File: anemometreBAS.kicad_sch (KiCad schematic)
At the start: 12 parts, among them J1 Conn_01x03_Male, J2 Conn_01x02_Male, J3 Conn_01x02_Male, J4 Conn_01x02_Male, J5 Conn_01x02_Male, U1 TP4056

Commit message: fix error
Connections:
- net 3V3: now also R1.1
- net at J1.1 (Pin_1): now also R1.2, XA1.A1; no longer R1.1
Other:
- moved on the sheet: R1
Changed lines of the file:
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@@
 (kicad_sch (version 20211123) (generator eeschema)
   (paper "A4")
+  (junction (at 100.33 86.36) (diameter 0) (color 0 0 0 0)
+  )
   (junction (at 34.29 76.2) (diameter 0) (color 0 0 0 0)
   )
@@
   (junction (at 199.39 55.88) (diameter 0) (color 0 0 0 0)
   )
+  (wire (pts (xy 90.17 86.36) (xy 92.71 86.36))
+    (stroke (width 0) (type default) (color 0 0 0 0))
+  )
+  (wire (pts (xy 199.39 55.88) (xy 208.28 55.88))
+    (stroke (width 0) (type default) (color 0 0 0 0))
+  )
+  (wire (pts (xy 76.2 113.03) (xy 83.82 113.03))
+    (stroke (width 0) (type default) (color 0 0 0 0))
+  )
+  (wire (pts (xy 34.29 60.96) (xy 34.29 66.04))
+    (stroke (width 0) (type default) (color 0 0 0 0))
+  )
+  (wire (pts (xy 205.74 58.42) (xy 208.28 58.42))
+    (stroke (width 0) (type default) (color 0 0 0 0))
+  )
+  (wire (pts (xy 34.29 76.2) (xy 38.1 76.2))
+    (stroke (width 0) (type default) (color 0 0 0 0))
+  )
+  (wire (pts (xy 118.11 109.22) (xy 123.19 109.22))
+    (stroke (width 0) (type default) (color 0 0 0 0))
+  )
+  (wire (pts (xy 34.29 86.36) (xy 34.29 91.44))
+    (stroke (width 0) (type default) (color 0 0 0 0))
+  )
+  (wire (pts (xy 101.6 104.14) (xy 123.19 104.14))
+    (stroke (width 0) (type default) (color 0 0 0 0))
+  )
+  (wire (pts (xy 76.2 115.57) (xy 83.82 115.57))
+    (stroke (width 0) (type default) (color 0 0 0 0))
+  )
+  (wire (pts (xy 120.65 78.74) (xy 123.19 78.74))
+    (stroke (width 0) (type default) (color 0 0 0 0))
+  )
+  (wire (pts (xy 80.01 125.73) (xy 83.82 125.73))
+    (stroke (width 0) (type default) (color 0 0 0 0))
+  )
+  (wire (pts (xy 97.79 64.77) (xy 97.79 67.31))
+    (stroke (width 0) (type default) (color 0 0 0 0))
+  )
+  (wire (pts (xy 120.65 73.66) (xy 123.19 73.66))
+    (stroke (width 0) (type default) (color 0 0 0 0))
+  )
+  (wire (pts (xy 189.23 55.88) (xy 199.39 55.88))
+    (stroke (width 0) (type default) (color 0 0 0 0))
+  )
+  (wire (pts (xy 60.96 40.64) (xy 60.96 44.45))
+    (stroke (width 0) (type default) (color 0 0 0 0))
+  )
+  (wire (pts (xy 199.39 40.64) (xy 199.39 48.26))
+    (stroke (width 0) (type default) (color 0 0 0 0))
+  )
+  (wire (pts (xy 72.39 128.27) (xy 83.82 128.27))
+    (stroke (width 0) (type default) (color 0 0 0 0))
+  )
+  (wire (pts (xy 109.22 106.68) (xy 123.19 106.68))
+    (stroke (width 0) (type default) (color 0 0 0 0))
+  )
+  (wire (pts (xy 85.09 40.64) (xy 85.09 38.1))
+    (stroke (width 0) (type default) (color 0 0 0 0))
+  )
+  (wire (pts (xy 95.25 64.77) (xy 95.25 72.39))
+    (stroke (width 0) (type default) (color 0 0 0 0))
+  )
+  (wire (pts (xy 60.96 120.65) (xy 83.82 120.65))
+    (stroke (width 0) (type default) (color 0 0 0 0))
+  )
+  (wire (pts (xy 118.11 101.6) (xy 123.19 101.6))
+    (stroke (width 0) (type default) (color 0 0 0 0))
+  )
+  (wire (pts (xy 85.09 40.64) (xy 85.09 44.45))
+    (stroke (width 0) (type default) (color 0 0 0 0))
+  )
+  (wire (pts (xy 60.96 118.11) (xy 83.82 118.11))
+    (stroke (width 0) (type default) (color 0 0 0 0))
+  )
+  (wire (pts (xy 34.29 73.66) (xy 34.29 76.2))
+    (stroke (width 0) (type default) (color 0 0 0 0))
+  )
+  (wire (pts (xy 34.29 76.2) (xy 34.29 78.74))
+    (stroke (width 0) (type default) (color 0 0 0 0))
+  )
+  (wire (pts (xy 63.5 40.64) (xy 85.09 40.64))
+    (stroke (width 0) (type default) (color 0 0 0 0))
+  )
+  (wire (pts (xy 85.09 25.4) (xy 85.09 30.48))
+    (stroke (width 0) (type default) (color 0 0 0 0))
+  )
+  (wire (pts (xy 100.33 64.77) (xy 100.33 86.36))
+    (stroke (width 0) (type default) (color 0 0 0 0))
+  )
   (wire (pts (xy 100.33 86.36) (xy 123.19 86.36))
-    (stroke (width 0) (type default) (color 0 0 0 0))
-  )
-  (wire (pts (xy 199.39 55.88) (xy 208.28 55.88))
-    (stroke (width 0) (type default) (color 0 0 0 0))
-  )
-  (wire (pts (xy 76.2 113.03) (xy 83.82 113.03))
-    (stroke (width 0) (type default) (color 0 0 0 0))
-  )
-  (wire (pts (xy 34.29 60.96) (xy 34.29 66.04))
-    (stroke (width 0) (type default) (color 0 0 0 0))
-  )
-  (wire (pts (xy 205.74 58.42) (xy 208.28 58.42))
-    (stroke (width 0) (type default) (color 0 0 0 0))
-  )
-  (wire (pts (xy 34.29 76.2) (xy 38.1 76.2))
-    (stroke (width 0) (type default) (color 0 0 0 0))
-  )
-  (wire (pts (xy 118.11 109.22) (xy 123.19 109.22))
-    (stroke (width 0) (type default) (color 0 0 0 0))
-  )
-  (wire (pts (xy 34.29 86.36) (xy 34.29 91.44))
-    (stroke (width 0) (type default) (color 0 0 0 0))
-  )
-  (wire (pts (xy 101.6 104.14) (xy 123.19 104.14))
-    (stroke (width 0) (type default) (color 0 0 0 0))
-  )
-  (wire (pts (xy 76.2 115.57) (xy 83.82 115.57))
-    (stroke (width 0) (type default) (color 0 0 0 0))
-  )
-  (wire (pts (xy 120.65 78.74) (xy 123.19 78.74))
-    (stroke (width 0) (type default) (color 0 0 0 0))
-  )
-  (wire (pts (xy 80.01 125.73) (xy 83.82 125.73))
-    (stroke (width 0) (type default) (color 0 0 0 0))
-  )
-  (wire (pts (xy 97.79 64.77) (xy 97.79 68.58))
-    (stroke (width 0) (type default) (color 0 0 0 0))
-  )
-  (wire (pts (xy 120.65 73.66) (xy 123.19 73.66))
-    (stroke (width 0) (type default) (color 0 0 0 0))
-  )
-  (wire (pts (xy 189.23 55.88) (xy 199.39 55.88))
-    (stroke (width 0) (type default) (color 0 0 0 0))
-  )
-  (wire (pts (xy 60.96 40.64) (xy 60.96 44.45))
-    (stroke (width 0) (type default) (color 0 0 0 0))
-  )
-  (wire (pts (xy 199.39 40.64) (xy 199.39 48.26))
-    (stroke (width 0) (type default) (color 0 0 0 0))
-  )
-  (wire (pts (xy 72.39 128.27) (xy 83.82 128.27))
-    (stroke (width 0) (type default) (color 0 0 0 0))
-  )
-  (wire (pts (xy 109.22 106.68) (xy 123.19 106.68))
-    (stroke (width 0) (type default) (color 0 0 0 0))
-  )
-  (wire (pts (xy 85.09 40.64) (xy 85.09 38.1))
-    (stroke (width 0) (type default) (color 0 0 0 0))
-  )
-  (wire (pts (xy 95.25 64.77) (xy 95.25 73.66))
-    (stroke (width 0) (type default) (color 0 0 0 0))
-  )
-  (wire (pts (xy 60.96 120.65) (xy 83.82 120.65))
-    (stroke (width 0) (type default) (color 0 0 0 0))
-  )
-  (wire (pts (xy 118.11 101.6) (xy 123.19 101.6))
-    (stroke (width 0) (type default) (color 0 0 0 0))
-  )
-  (wire (pts (xy 85.09 40.64) (xy 85.09 44.45))
-    (stroke (width 0) (type default) (color 0 0 0 0))
-  )
-  (wire (pts (xy 60.96 118.11) (xy 83.82 118.11))
-    (stroke (width 0) (type default) (color 0 0 0 0))
-  )
-  (wire (pts (xy 34.29 73.66) (xy 34.29 76.2))
-    (stroke (width 0) (type default) (color 0 0 0 0))
-  )
-  (wire (pts (xy 34.29 76.2) (xy 34.29 78.74))
-    (stroke (width 0) (type default) (color 0 0 0 0))
-  )
-  (wire (pts (xy 100.33 64.77) (xy 100.33 78.74))
-    (stroke (width 0) (type default) (color 0 0 0 0))
-  )
-  (wire (pts (xy 63.5 40.64) (xy 85.09 40.64))
-    (stroke (width 0) (type default) (color 0 0 0 0))
-  )
-  (wire (pts (xy 85.09 25.4) (xy 85.09 30.48))
     (stroke (width 0) (type default) (color 0 0 0 0))
   )
@@
     )
   )
+  (global_label "3V3" (shape input) (at 90.17 86.36 180) (fields_autoplaced)
+    (effects (font (size 1.27 1.27)) (justify right))
+    (property "Intersheet References" "${INTERSHEET_REFS}" (id 0) (at 84.2493 86.4394 0)
+      (effects (font (size 1.27 1.27)) (justify left) hide)
+    )
+  )
   (global_label "VIN" (shape input) (at 80.01 125.73 180) (fields_autoplaced)
     (effects (font (size 1.27 1.27)) (justify right))
@@
     )
   )
-  (global_label "5V" (shape input) (at 97.79 68.58 270) (fields_autoplaced)
-    (effects (font (size 1.27 1.27)) (justify right))
-    (property "Intersheet References" "${INTERSHEET_REFS}" (id 0) (at 97.8694 73.2912 90)
+  (global_label "5V" (shape input) (at 97.79 67.31 270) (fields_autoplaced)
+    (effects (font (size 1.27 1.27)) (justify right))
+    (property "Intersheet References" "${INTERSHEET_REFS}" (id 0) (at 97.8694 72.0212 90)
       (effects (font (size 1.27 1.27)) (justify left) hide)
     )
@@
     )
   )
-  (global_label "GND" (shape input) (at 95.25 73.66 270) (fields_autoplaced)
-    (effects (font (size 1.27 1.27)) (justify right))
-    (property "Intersheet References" "${INTERSHEET_REFS}" (id 0) (at 95.3294 79.9436 90)
+  (global_label "GND" (shape input) (at 95.25 72.39 270) (fields_autoplaced)
+    (effects (font (size 1.27 1.27)) (justify right))
+    (property "Intersheet References" "${INTERSHEET_REFS}" (id 0) (at 95.3294 78.6736 90)
       (effects (font (size 1.27 1.27)) (justify left) hide)
     )
@@
     (pin "2")
   )
-  (symbol (lib_id "Device:R") (at 100.33 82.55 0) (unit 1)
-    (in_bom yes) (on_board yes) (fields_autoplaced)
-    (property "Reference" "R1" (id 0) (at 102.87 81.2799 0)
-      (effects (font (size 1.27 1.27)) (justify left))
-    )
-    (property "Value" "4.7K" (id 1) (at 102.87 83.8199 0)
-      (effects (font (size 1.27 1.27)) (justify left))
-    )
-    (property "Footprint" "" (id 2) (at 98.552 82.55 90)
-      (effects (font (size 1.27 1.27)) hide)
-    )
-    (property "Datasheet" "~" (id 3) (at 100.33 82.55 0)
-      (effects (font (size 1.27 1.27)) hide)
-    )
+  (symbol (lib_id "Device:R") (at 96.52 86.36 90) (unit 1)
+    (in_bom yes) (on_board yes) (fields_autoplaced)
+    (property "Reference" "R1" (id 0) (at 96.52 80.01 90))
+    (property "Value" "4.7K" (id 1) (at 96.52 82.55 90))
+    (property "Footprint" "" (id 2) (at 96.52 88.138 90)
+      (effects (font (size 1.27 1.27)) hide)
+    )
+    (property "Datasheet" "~" (id 3) (at 96.52 86.36 0)
+      (effects (font (size 1.27 1.27)) hide)
+    )

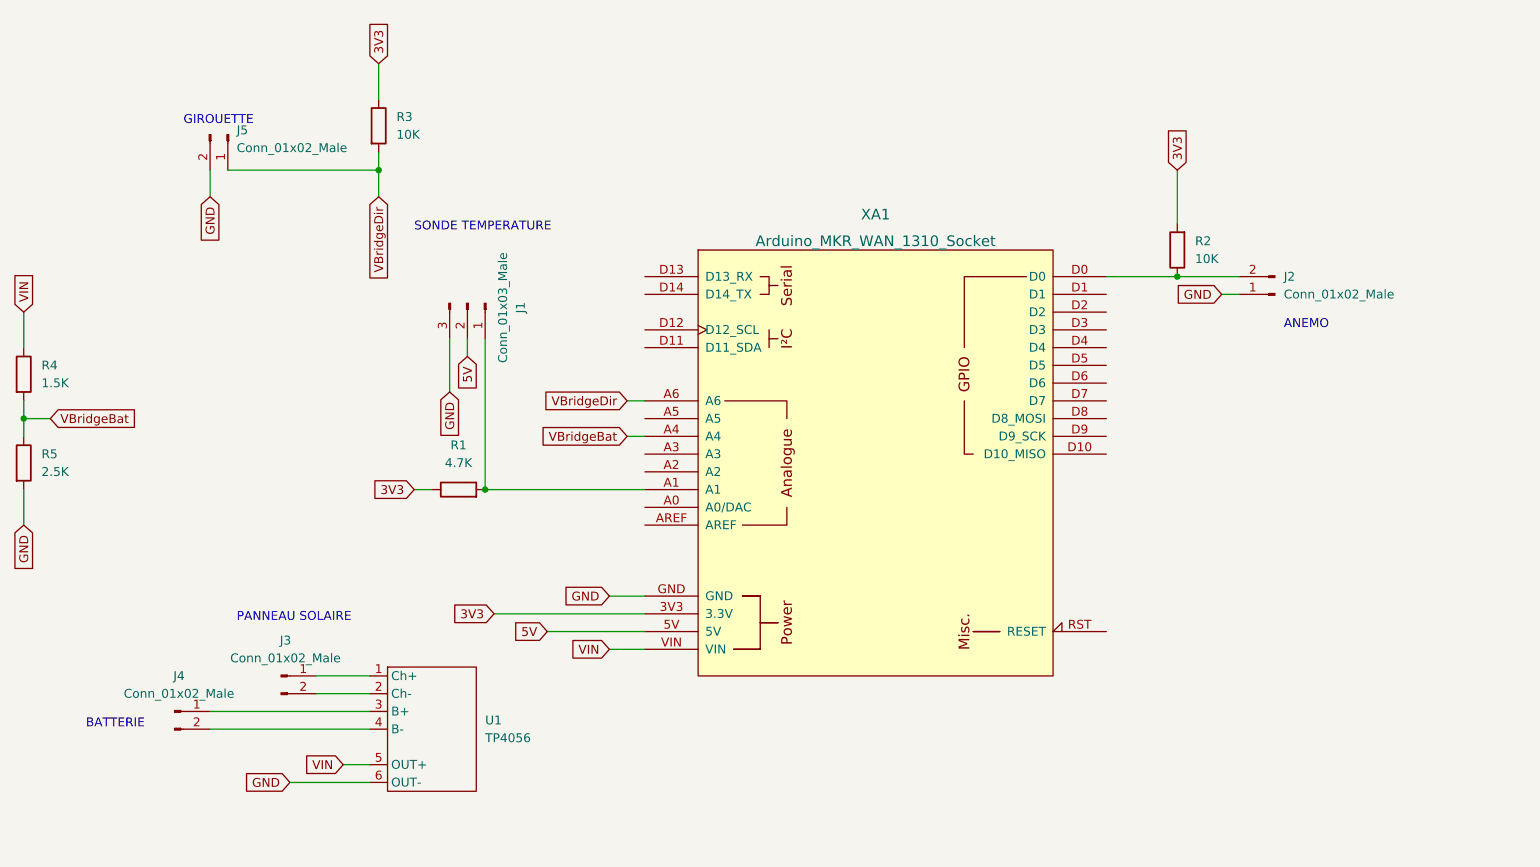
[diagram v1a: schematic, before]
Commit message: Pcb traversant (#1)
* first pcb version with schematic footprint update

* schematic
	GND at the same pin for each connector
	add M3 hole*3 connected to GND
PCB
	first routing

* Adding 3D model

* route temp sensor data
change +5V net location
change hole location
drc ok only one error with hole under mkr processing board

* pcb without smd resistor
first routing version

* change layer of solar panel and battery mngt card
unshow $Reference and value

* Adding pins socket connectors for MKR1310

* adding optionnal CEM schottky diode
MKR 3D model update

* update 3D models with MKR pin shocket

---------

Co-authored-by: sdaviet <sylvain.daviet@gmail.com>
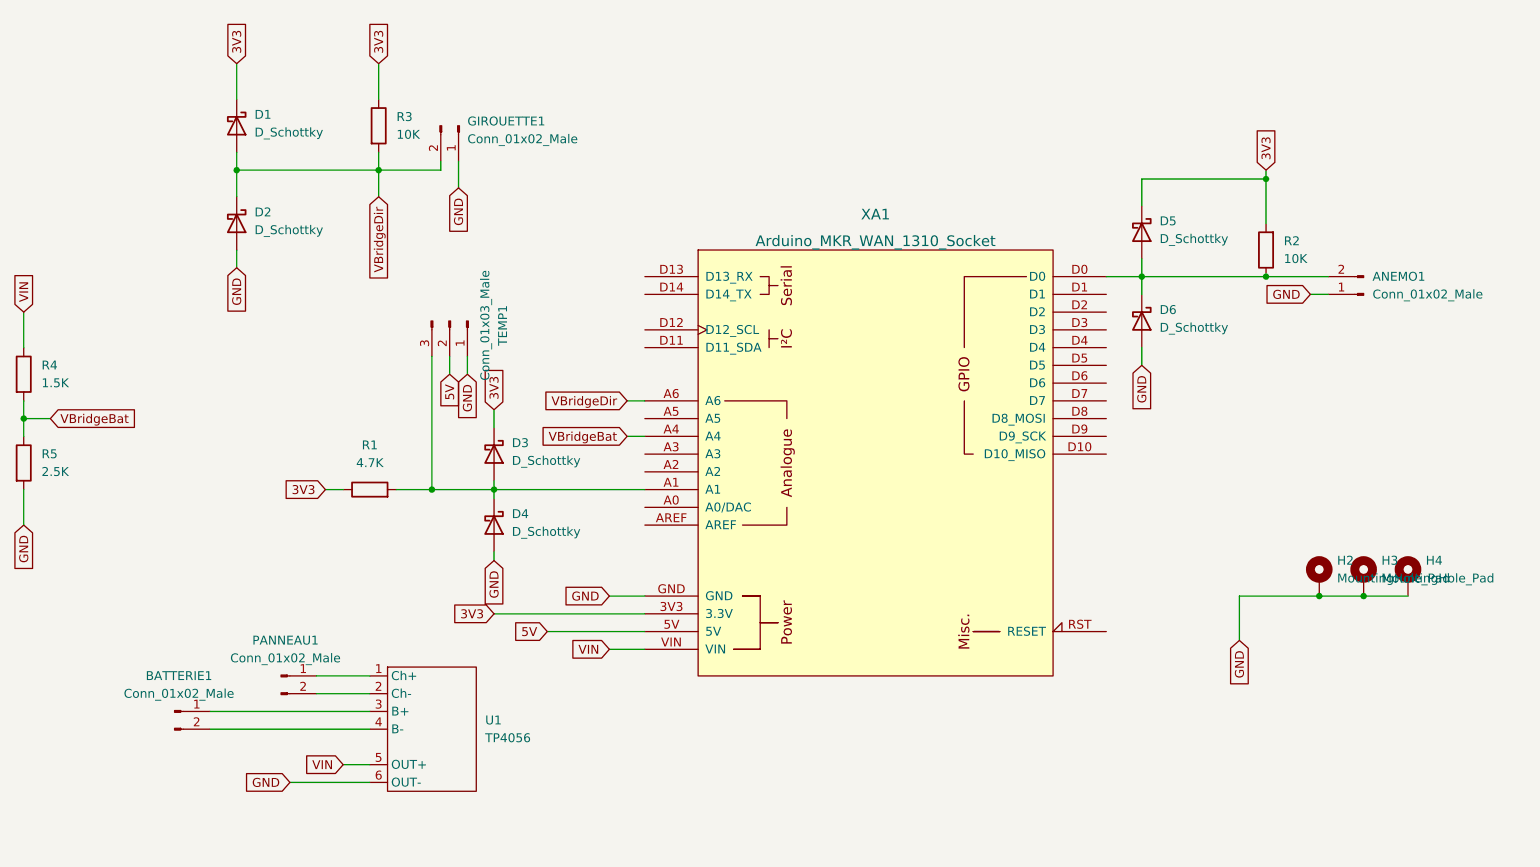
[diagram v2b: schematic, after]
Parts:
- added D1, D2, D3, D4, D5, D6: D_Schottky, Diode_THT:D_DO-35_SOD27_P7.62mm_Horizontal, symbol Device:D_Schottky
- added H2, H3, H4: MountingHole_Pad, MountingHole:MountingHole_3.2mm_M3_Pad_TopBottom, symbol Mechanical:MountingHole_Pad
- ANEMO1: renamed from J2; footprint (none) -> Connector_JST:JST_XH_B3B-XH-A_1x03_P2.50mm_Vertical
- BATTERIE1: renamed from J4; footprint (none) -> Connector_JST:JST_XH_B2B-XH-A_1x02_P2.50mm_Vertical
- GIROUETTE1: renamed from J5; footprint (none) -> Connector_JST:JST_XH_B3B-XH-A_1x03_P2.50mm_Vertical
- PANNEAU1: renamed from J3; footprint (none) -> Connector_JST:JST_XH_B2B-XH-A_1x02_P2.50mm_Vertical
- R1, R2, R3, R4, R5: footprint (none) -> Resistor_THT:R_Axial_DIN0204_L3.6mm_D1.6mm_P7.62mm_Horizontal
- TEMP1: renamed from J1; footprint (none) -> Connector_JST:JST_XH_B3B-XH-A_1x03_P2.50mm_Vertical
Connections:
- net 3V3: now also D1.1 (K), D3.1 (K), D5.1 (K)
- net GND: now also GIROUETTE1.1 (Pin_1), TEMP1.1 (Pin_1), D2.2 (A), D4.2 (A), D6.2 (A), H2.1, H3.1, H4.1; no longer GIROUETTE1.2 (Pin_2), TEMP1.3 (Pin_3)
- net VBridgeDir: now also GIROUETTE1.2 (Pin_2), D1.2 (A), D2.1 (K); no longer GIROUETTE1.1 (Pin_1)
- net at R1.2, XA1.A1: now also TEMP1.3 (Pin_3), D3.2 (A), D4.1 (K); no longer TEMP1.1 (Pin_1)
- net at ANEMO1.2 (Pin_2), R2.1, XA1.D0: now also D5.2 (A), D6.1 (K)
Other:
- note removed: "ANEMO"
- note removed: "BATTERIE"
- note removed: "GIROUETTE"
- note removed: "PANNEAU SOLAIRE"
- note removed: "SONDE TEMPERATURE"
- moved on the sheet: ANEMO1, GIROUETTE1, R1, R2, TEMP1

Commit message: Fix power issue
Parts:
- added J6: Power, symbol Connector:Conn_01x02_Male
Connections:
- net 3V3: now also TEMP1.2 (Pin_2)
- net 5V: no longer TEMP1.2 (Pin_2)
- net GND: now also J6.2 (Pin_2)
- net B+: now reaches BATTERIE1.1 (Pin_1), U1.3 (B+)
- net B+: now also R4.1
- removed net VIN: R4.1, U1.5 (OUT+), XA1.VIN
- new net: J6.1 (Pin_1), U1.5 (OUT+)

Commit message: add power connector as jst routing pcb
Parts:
- J6: footprint (none) -> Connector_JST:JST_XH_B2B-XH-A_1x02_P2.50mm_Vertical
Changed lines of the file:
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@@
     (property "Reference" "J6" (id 0) (at 56.515 120.65 0))
     (property "Value" "Power" (id 1) (at 56.515 123.19 0))
-    (property "Footprint" "" (id 2) (at 55.88 125.73 0)
+    (property "Footprint" "Connector_JST:JST_XH_B2B-XH-A_1x02_P2.50mm_Vertical" (id 2) (at 55.88 125.73 0)
       (effects (font (size 1.27 1.27)) hide)
     )
@@
     )
     (path "/7d74f531-c792-4beb-b3ab-45711ef608ce"
-      (reference "J6") (unit 1) (value "Power") (footprint "")
+      (reference "J6") (unit 1) (value "Power") (footprint "Connector_JST:JST_XH_B2B-XH-A_1x02_P2.50mm_Vertical")
     )
     (path "/3c744949-20c9-495f-819b-b231fc469afd"
